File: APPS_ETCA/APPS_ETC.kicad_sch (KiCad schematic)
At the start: 21 parts, among them P1 DTM1312PC12PDR008, U1 NSL-32, U2 DK1A1B-12V, U3 NSL-32, U4 DK1A1B-12V, U6 MCP6004 - BUFFER

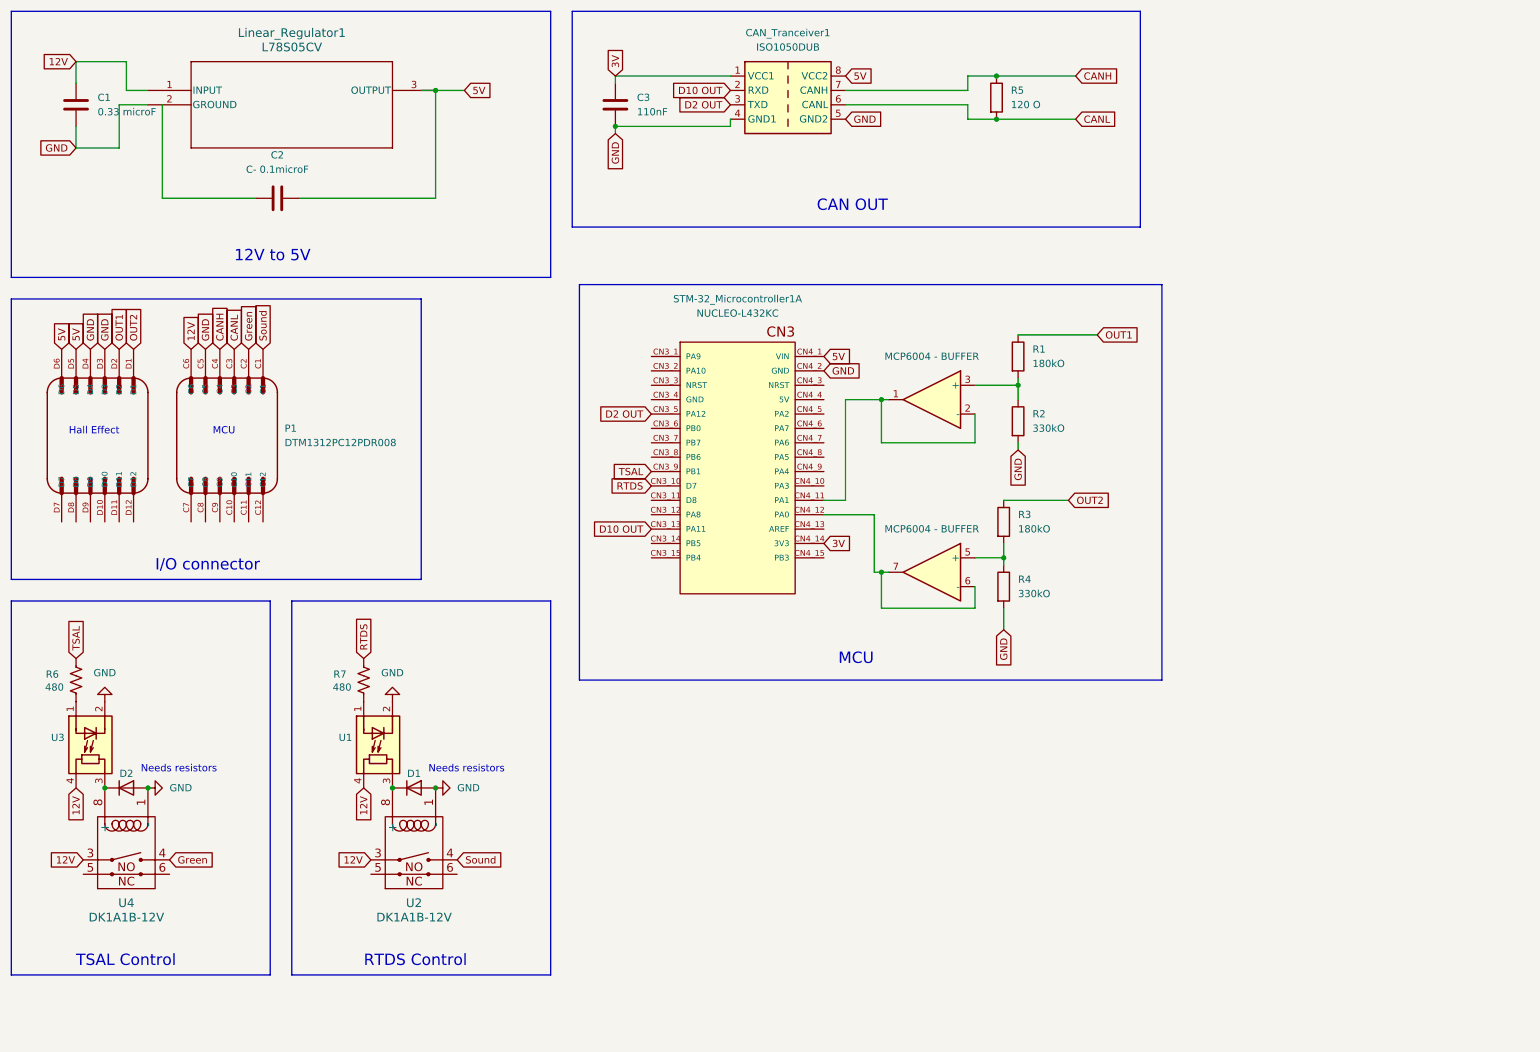
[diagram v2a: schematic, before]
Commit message: updated lin reg, v div etc.
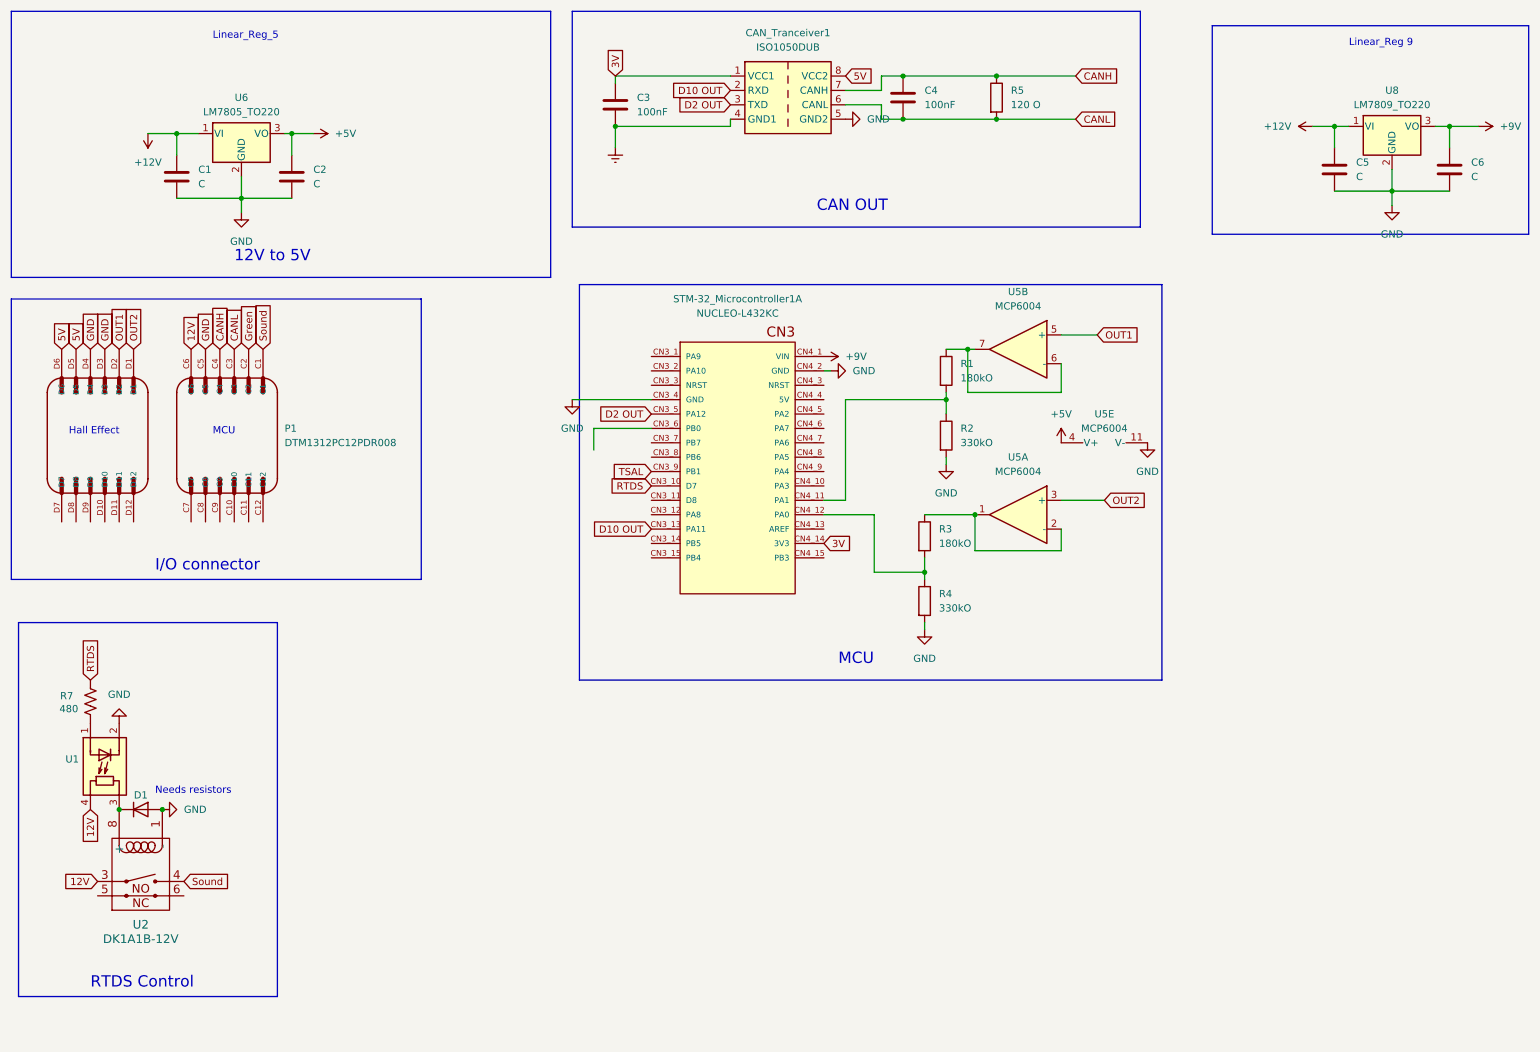
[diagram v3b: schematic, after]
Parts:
- removed D2: D, Diode_THT:D_DO-41_SOD81_P10.16mm_Horizontal, symbol Device:D
- removed Linear_Regulator1: L78S05CV, TO-220_STM, symbol Regulator_Linear:L78S05CV
- removed R6: 480, Resistor_THT:R_Axial_DIN0207_L6.3mm_D2.5mm_P10.16mm_Horizontal, symbol Device:R_US
- removed U3: NSL-32, 1FS_2_Global_Footprint_Library:OptoCoupler 6-SOP, symbol Isolator:NSL-32
- removed U4: DK1A1B-12V, 1FS_2_Global_Footprint_Library:RELAY_DK2A_PAN, symbol 2FS-1_Symbol Library:DK1A1B-12V
- removed U6: MCP6004 - BUFFER, symbol Amplifier_Operational:MCP6004
- added C4: 100nF, symbol Device:C
- added C5, C6: C, symbol Device:C
- added U5: MCP6004, symbol Amplifier_Operational:MCP6004
- added U6: LM7805_TO220, Package_TO_SOT_THT:TO-220-3_Vertical, symbol Regulator_Linear:LM7805_TO220
- added U8: LM7809_TO220, Package_TO_SOT_THT:TO-220-3_Vertical, symbol Regulator_Linear:LM7809_TO220
- C1: value 0.33 microF -> C
- C2: value C- 0.1microF -> C
- C3: value 110nF -> 100nF
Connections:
- net 12V: no longer C1.1
- net 5V: no longer C2.2, STM-32_Microcontroller1.CN4_1 (VIN)
- net CANH: now also C4.1
- net CANL: now also C4.2
- net GND: now also C2.2, STM-32_Microcontroller1.CN3_4 (GND), C5.2, C6.2, U5.11 (V-), U6.2 (GND), U8.2 (GND); no longer C3.2, CAN_Tranceiver1.4 (GND1)
- net OUT1: now also U5.5 (+); no longer R1.1
- net OUT2: now also U5.3 (+); no longer R3.1
- net at R3.2, R4.1: now also STM-32_Microcontroller1.CN4_12 (PA0)
- net +5V: now reaches C2.1
- net +5V: now also U5.4 (V+), U6.3 (VO)
- net at R1.2, R2.1: now also STM-32_Microcontroller1.CN4_11 (PA1)
- new net: R3.1, U5.1, U5.2 (-)
- new net: R1.1, U5.6 (-), U5.7
- new net +12V: C1.1, C5.1, U6.1 (VI), U8.1 (VI)
- new net +9V: C6.1, STM-32_Microcontroller1.CN4_1 (VIN), U8.3 (VO)
- new net Earth: C3.2, CAN_Tranceiver1.4 (GND1)
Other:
- note added: "Linear_Reg 9"
- note added: "Linear_Reg_5"
- note removed: "TSAL Control"
- moved on the sheet: D1, R7, U1, U2

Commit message: started PCB
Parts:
- removed U5: MCP6004, symbol Amplifier_Operational:MCP6004
- added U3: MCP6004, FSFootprints:PDIP14_300MC_MCH, symbol Amplifier_Operational:MCP6004
- C1: value C -> 0.33 mF; footprint (none) -> Capacitor_SMD:C_0805_2012Metric_Pad1.18x1.45mm_HandSolder
- C2, C6: value C -> 0.1 mF; footprint (none) -> Capacitor_SMD:C_0805_2012Metric_Pad1.18x1.45mm_HandSolder
- C3, C4: footprint (none) -> Capacitor_SMD:C_0805_2012Metric_Pad1.18x1.45mm_HandSolder
- C5: value C -> 0.33mF; footprint (none) -> Capacitor_SMD:C_0805_2012Metric_Pad1.18x1.45mm_HandSolder
- P1: footprint DTM1312PC12PDR008:TE_DTM1312PC12PDR008 -> 1FS_2_Global_Footprint_Library:TE_DTM1312PC12PDR008
- R1, R2, R3, R4, R5: footprint (none) -> Resistor_SMD:R_0805_2012Metric_Pad1.20x1.40mm_HandSolder
- R7: footprint Resistor_THT:R_Axial_DIN0207_L6.3mm_D2.5mm_P10.16mm_Horizontal -> Resistor_SMD:R_0805_2012Metric_Pad1.20x1.40mm_HandSolder
- STM-32_Microcontroller1: footprint NUCLEO-L432KC:MODULE_NUCLEO-L432KC -> 1FS_2_Global_Footprint_Library:MODULE_NUCLEO-L432KC
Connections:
- net +5V: now also U3.4 (V+)
- net GND: now also U3.11 (V-)
- net OUT1: now also U3.2 (-)
- net OUT2: now also U3.6 (-)
- net at R3.1: now also U3.5 (+), U3.7
- net at R1.1: now also U3.1, U3.3 (+)

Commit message: board layout w connectors
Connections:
- net 12V: now also P1.D6; no longer P1.C6
- net 5V: now also P1.C4, P1.C6; no longer P1.D5, P1.D6
- net CANH: now also P1.D4; no longer P1.C4
- net CANL: now also P1.D3; no longer P1.C3
- net GND: now also P1.C3, P1.D5; no longer P1.D3, P1.D4
- net Green: now also P1.D2; no longer P1.C2
- net OUT1: now also P1.C2; no longer P1.D2
- net OUT2: now also P1.C1; no longer P1.D1
- net Sound: now also P1.D1; no longer P1.C1
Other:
- note added: "Hall effect"
- note removed: "Hall Effect"
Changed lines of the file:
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@@
     (effects (font (size 2 2)) (justify left bottom))
   )
-  (text "MCU\n" (at 50.8 90.17 0)
+  (text "Hall effect\n\n" (at 50.8 90.17 0)
     (effects (font (size 1.27 1.27)) (justify left bottom))
   )
@@
     (effects (font (size 2 2)) (justify left bottom))
   )
-  (text "Hall Effect" (at 25.4 90.17 0)
+  (text "MCU\n" (at 25.4 90.17 0)
     (effects (font (size 1.27 1.27)) (justify left bottom))
   )
@@
     (effects (font (size 2 2)) (justify left bottom))
   )
-  (global_label "Green" (shape input) (at 57.15 74.93 90) (fields_autoplaced)
+  (global_label "Green" (shape input) (at 34.29 74.93 90) (fields_autoplaced)
     (effects (font (size 1.27 1.27)) (justify left))
-    (property "Intersheetrefs" "${INTERSHEET_REFS}" (at 57.15 66.5624 90)
+    (property "Intersheetrefs" "${INTERSHEET_REFS}" (at 34.29 66.5624 90)
       (effects (font (size 1.27 1.27)) (justify left) hide)
     )
@@
     (property "Intersheetrefs" "${INTERSHEET_REFS}" (at 29.21 162.7028 90)
       (effects (font (size 1.27 1.27)) (justify right) hide)
+    )
+  )
+  (global_label "GND" (shape input) (at 54.61 74.93 90) (fields_autoplaced)
+    (effects (font (size 1.27 1.27)) (justify left))
+    (property "Intersheetrefs" "${INTERSHEET_REFS}" (at 54.61 68.0743 90)
+      (effects (font (size 1.27 1.27)) (justify left) hide)
     )
   )
@@
     )
   )
-  (global_label "OUT2" (shape input) (at 36.83 74.93 90) (fields_autoplaced)
-    (effects (font (size 1.27 1.27)) (justify left))
-    (property "Intersheetrefs" "${INTERSHEET_REFS}" (at 36.83 67.1067 90)
-      (effects (font (size 1.27 1.27)) (justify left) hide)
-    )
-  )
-  (global_label "GND" (shape input) (at 31.75 74.93 90) (fields_autoplaced)
-    (effects (font (size 1.27 1.27)) (justify left))
-    (property "Intersheetrefs" "${INTERSHEET_REFS}" (at 31.75 68.0743 90)
-      (effects (font (size 1.27 1.27)) (justify left) hide)
-    )
-  )
   (global_label "12V" (shape input) (at 30.48 168.91 180) (fields_autoplaced)
     (effects (font (size 1.27 1.27)) (justify right))
@@
     )
   )
-  (global_label "GND" (shape input) (at 49.53 74.93 90) (fields_autoplaced)
+  (global_label "GND" (shape input) (at 26.67 74.93 90) (fields_autoplaced)
     (effects (font (size 1.27 1.27)) (justify left))
-    (property "Intersheetrefs" "${INTERSHEET_REFS}" (at 49.53 68.0743 90)
+    (property "Intersheetrefs" "${INTERSHEET_REFS}" (at 26.67 68.0743 90)
       (effects (font (size 1.27 1.27)) (justify left) hide)
     )
@@
     )
   )
-  (global_label "12V" (shape input) (at 46.99 74.93 90) (fields_autoplaced)
+  (global_label "12V" (shape input) (at 24.13 74.93 90) (fields_autoplaced)
     (effects (font (size 1.27 1.27)) (justify left))
-    (property "Intersheetrefs" "${INTERSHEET_REFS}" (at 46.99 68.4372 90)
+    (property "Intersheetrefs" "${INTERSHEET_REFS}" (at 24.13 68.4372 90)
       (effects (font (size 1.27 1.27)) (justify left) hide)
     )
@@
     )
   )
-  (global_label "Sound" (shape input) (at 59.69 74.93 90) (fields_autoplaced)
+  (global_label "GND" (shape input) (at 49.53 74.93 90) (fields_autoplaced)
     (effects (font (size 1.27 1.27)) (justify left))
-    (property "Intersheetrefs" "${INTERSHEET_REFS}" (at 59.69 66.1393 90)
+    (property "Intersheetrefs" "${INTERSHEET_REFS}" (at 49.53 68.0743 90)
+      (effects (font (size 1.27 1.27)) (justify left) hide)
+    )
+  )
+  (global_label "Sound" (shape input) (at 36.83 74.93 90) (fields_autoplaced)
+    (effects (font (size 1.27 1.27)) (justify left))
+    (property "Intersheetrefs" "${INTERSHEET_REFS}" (at 36.83 66.1393 90)
+      (effects (font (size 1.27 1.27)) (justify left) hide)
+    )
+  )
+  (global_label "5V" (shape input) (at 46.99 74.93 90) (fields_autoplaced)
+    (effects (font (size 1.27 1.27)) (justify left))
+    (property "Intersheetrefs" "${INTERSHEET_REFS}" (at 46.99 69.6467 90)
+      (effects (font (size 1.27 1.27)) (justify left) hide)
+    )
+  )
+  (global_label "5V" (shape input) (at 52.07 74.93 90) (fields_autoplaced)
+    (effects (font (size 1.27 1.27)) (justify left))
+    (property "Intersheetrefs" "${INTERSHEET_REFS}" (at 52.07 69.6467 90)
       (effects (font (size 1.27 1.27)) (justify left) hide)
     )
@@
     )
   )
-  (global_label "5V" (shape input) (at 26.67 74.93 90) (fields_autoplaced)
+  (global_label "OUT2" (shape input) (at 59.69 74.93 90) (fields_autoplaced)
     (effects (font (size 1.27 1.27)) (justify left))
-    (property "Intersheetrefs" "${INTERSHEET_REFS}" (at 26.67 69.6467 90)
-      (effects (font (size 1.27 1.27)) (justify left) hide)
-    )
-  )
-  (global_label "5V" (shape input) (at 24.13 74.93 90) (fields_autoplaced)
-    (effects (font (size 1.27 1.27)) (justify left))
-    (property "Intersheetrefs" "${INTERSHEET_REFS}" (at 24.13 69.6467 90)
+    (property "Intersheetrefs" "${INTERSHEET_REFS}" (at 59.69 67.1067 90)
       (effects (font (size 1.27 1.27)) (justify left) hide)
     )
@@
     (effects (font (size 1.27 1.27)) (justify left))
     (property "Intersheetrefs" "${INTERSHEET_REFS}" (at 210.9024 34.29 0)
-      (effects (font (size 1.27 1.27)) (justify left) hide)
-    )
-  )
-  (global_label "GND" (shape input) (at 29.21 74.93 90) (fields_autoplaced)
-    (effects (font (size 1.27 1.27)) (justify left))
-    (property "Intersheetrefs" "${INTERSHEET_REFS}" (at 29.21 68.0743 90)
       (effects (font (size 1.27 1.27)) (justify left) hide)
     )
@@
     )
   )
-  (global_label "CANH" (shape input) (at 52.07 74.93 90) (fields_autoplaced)
+  (global_label "CANH" (shape input) (at 29.21 74.93 90) (fields_autoplaced)
     (effects (font (size 1.27 1.27)) (justify left))
-    (property "Intersheetrefs" "${INTERSHEET_REFS}" (at 52.07 66.9252 90)
+    (property "Intersheetrefs" "${INTERSHEET_REFS}" (at 29.21 66.9252 90)
       (effects (font (size 1.27 1.27)) (justify left) hide)
     )
@@
     )
   )
-  (global_label "CANL" (shape input) (at 54.61 74.93 90) (fields_autoplaced)
+  (global_label "OUT1" (shape input) (at 57.15 74.93 90) (fields_autoplaced)
     (effects (font (size 1.27 1.27)) (justify left))
-    (property "Intersheetrefs" "${INTERSHEET_REFS}" (at 54.61 67.2276 90)
+    (property "Intersheetrefs" "${INTERSHEET_REFS}" (at 57.15 67.1067 90)
       (effects (font (size 1.27 1.27)) (justify left) hide)
     )
   )
-  (global_label "OUT1" (shape input) (at 34.29 74.93 90) (fields_autoplaced)
+  (global_label "CANL" (shape input) (at 31.75 74.93 90) (fields_autoplaced)
     (effects (font (size 1.27 1.27)) (justify left))
-    (property "Intersheetrefs" "${INTERSHEET_REFS}" (at 34.29 67.1067 90)
+    (property "Intersheetrefs" "${INTERSHEET_REFS}" (at 31.75 67.2276 90)
       (effects (font (size 1.27 1.27)) (justify left) hide)
     )

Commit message: updated schema
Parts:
- removed D1: D, Diode_THT:D_DO-41_SOD81_P10.16mm_Horizontal, symbol Device:D
- removed R7: 480, Resistor_SMD:R_0805_2012Metric_Pad1.20x1.40mm_HandSolder, symbol Device:R_US
- removed U1: NSL-32, 1FS_2_Global_Footprint_Library:OptoCoupler 6-SOP, symbol Isolator:NSL-32
- removed U2: DK1A1B-12V, 1FS_2_Global_Footprint_Library:RELAY_DK2A_PAN, symbol 2FS-1_Symbol Library:DK1A1B-12V
- added CR1: STS6NF20V, 1FS_2_Global_Footprint_Library:SOIC127P600X175-8N, symbol 1FS_2_Global_Symbol_Library:STS6NF20V
- added D1: LED, LED_THT:LED_D10.0mm, symbol Device:LED
- added R6: 10 ohm, Resistor_SMD:R_0805_2012Metric_Pad1.20x1.40mm_HandSolder, symbol Device:R
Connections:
- net 12V is gone; now on net +12V: P1.D6
- net Earth is gone; now on net GND: C3.2, CAN_Tranceiver1.4 (GND1)
- net Green is gone; now on net +12V: P1.D2
- net +5V: now also CAN_Tranceiver1.8 (VCC2), P1.C12, P1.C9
- net GND: now also P1.C11, P1.C8, CR1.1 (S), CR1.2 (S), CR1.3 (S), D1.1 (K); no longer P1.C3, P1.C5
- net OUT1: no longer P1.C2
- net OUT2: now also P1.C7; no longer P1.C1
- net Brake Sensor: now reaches P1.D7
- net Brake Sensor: now also STM-32_Microcontroller1.CN4_10 (PA3)
- net LED: now reaches STM-32_Microcontroller1.CN3_6 (PB0)
- net LED: now also R6.2
- net 3V renamed +3.3V
- removed net 5V: CAN_Tranceiver1.8 (VCC2), P1.C4, P1.C6
- net RTDS renamed RTDS Control
- net RTDS Control: now also CR1.4 (G)
- net Sound renamed RTDS GND
- net RTDS GND: now also CR1.5 (D), CR1.6 (D), CR1.7 (D), CR1.8 (D)
- net TSAL: no longer names the net of STM-32_Microcontroller1.CN3_9 (PB1)
- new net: D1.2 (A), R6.1
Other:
- note removed: "Needs resistors"
- moved on the sheet: C1, C2, C5, C6, P1, R1, R2, R3, R4, STM-32_Microcontroller1A, U3A, U3B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

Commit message: for my colead abhi <3
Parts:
- removed D1: LED, LED_THT:LED_D10.0mm, symbol Device:LED
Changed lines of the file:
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@@
-    )
-  )
-  (symbol (lib_id "Device:LED") (at 139.7 104.14 180) (unit 1)
-    (in_bom yes) (on_board yes) (dnp no) (fields_autoplaced)
-    (property "Reference" "D1" (at 141.2875 96.52 0)
-      (effects (font (size 1.27 1.27)))
-    )
-    (property "Value" "LED" (at 141.2875 99.06 0)
-      (effects (font (size 1.27 1.27)))
-    )
-    (property "Footprint" "LED_THT:LED_D10.0mm" (at 139.7 104.14 0)
-      (effects (font (size 1.27 1.27)) hide)
-    )
-    (property "Datasheet" "~" (at 139.7 104.14 0)
-      (effects (font (size 1.27 1.27)) hide)
-    )
-    (pin "1")
-    (pin "2")
-    (instances
-      (project "APPS_ETC"
-        (path "/21da8b0a-bf7f-4003-9579-5de7190091be"
-          (reference "D1") (unit 1)
-        )
-      )
     )
   )

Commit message: Linear Reg. CAN. All that
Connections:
- net OUT1: now also P1.C10
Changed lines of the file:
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@@
+    (stroke (width 0) (type default))
+  )
+  (wire (pts (xy 132.08 180.34) (xy 132.08 187.96))
     (stroke (width 0) (type default))
   )
